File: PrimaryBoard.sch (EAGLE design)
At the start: 29 parts, among them J10 LORA32U4II, J11 CONN_42.54_SCREW, J13 POWER_JACK, J4 CONN_32.54_SCREW, J5 CONN_32.54_SCREW, J6 CONN_32.54_SCREW, J7 CONN_32.54_SCREW, J8 CONN_32.54_SCREW, J9 CONN_32.54_SCREW, U1 CD74HC4052PW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

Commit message: Minor updates and cleanup for primary board
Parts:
- added R2, R3: 10k, bschulz:R-EU_R0805
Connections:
- net 3V3_CORE: now also R2.2, R3.2
- net SCL: now also R3.1
- net SDA: now also R2.1
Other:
- note removed: "I2C Pullups!"
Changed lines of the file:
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@@
 <part name="C6" library="bschulz_passives" deviceset="C-EU" device="C0805"/>
 <part name="GND10" library="supply1" library_urn="urn:adsk.eagle:library:371" deviceset="GND" device=""/>
+<part name="R2" library="bschulz" deviceset="R-EU_" device="R0805" value="10k"/>
+<part name="R3" library="bschulz" deviceset="R-EU_" device="R0805" value="10k"/>
 </parts>
 <sheets>
 <sheet>
 <plain>
-<text x="78.74" y="102.87" size="1.778" layer="91">S0
+<text x="78.74" y="107.95" size="1.778" layer="91">S0
 S1
 IO_EN
@@
 LORA_EN
 5V_EXT_SENSE</text>
-<text x="78.74" y="99.06" size="1.778" layer="91">I2C Pullups!</text>
 </plain>
 <instances>
@@
 <instance part="GND10" gate="1" x="106.68" y="86.36" smashed="yes">
 <attribute name="VALUE" x="104.14" y="83.82" size="1.778" layer="96"/>
+</instance>
+<instance part="R2" gate="G$1" x="177.8" y="78.74" smashed="yes" rot="R90">
+<attribute name="NAME" x="176.3014" y="74.93" size="1.778" layer="95" rot="R90"/>
+<attribute name="VALUE" x="181.102" y="74.93" size="1.778" layer="96" rot="R90"/>
+</instance>
+<instance part="R3" gate="G$1" x="185.42" y="78.74" smashed="yes" rot="R90">
+<attribute name="NAME" x="183.9214" y="74.93" size="1.778" layer="95" rot="R90"/>
+<attribute name="VALUE" x="188.722" y="74.93" size="1.778" layer="96" rot="R90"/>
 </instance>
 </instances>
@@
 <wire x1="106.68" y1="99.06" x2="111.76" y2="99.06" width="0.1524" layer="91"/>
 </segment>
+<segment>
+<pinref part="R2" gate="G$1" pin="2"/>
+<wire x1="177.8" y1="83.82" x2="177.8" y2="86.36" width="0.1524" layer="91"/>
+<wire x1="177.8" y1="86.36" x2="185.42" y2="86.36" width="0.1524" layer="91"/>
+<pinref part="R3" gate="G$1" pin="2"/>
+<wire x1="185.42" y1="86.36" x2="185.42" y2="83.82" width="0.1524" layer="91"/>
+<wire x1="185.42" y1="86.36" x2="190.5" y2="86.36" width="0.1524" layer="91"/>
+<junction x="185.42" y="86.36"/>
+<label x="190.5" y="86.36" size="1.778" layer="95" xref="yes"/>
+</segment>
 </net>
 <net name="3V3_EXT" class="0">
@@
 <label x="129.54" y="83.82" size="1.778" layer="95"/>
 </segment>
+<segment>
+<pinref part="R2" gate="G$1" pin="1"/>
+<wire x1="177.8" y1="73.66" x2="177.8" y2="71.12" width="0.1524" layer="91"/>
+<wire x1="177.8" y1="71.12" x2="170.18" y2="71.12" width="0.1524" layer="91"/>
+<label x="170.18" y="71.12" size="1.778" layer="95"/>
+</segment>
 </net>
 <net name="SCL" class="0">
@@
 <label x="129.54" y="88.9" size="1.778" layer="95"/>
 </segment>
-</net>
+<segment>
+<pinref part="R3" gate="G$1" pin="1"/>
+<wire x1="185.42" y1="73.66" x2="185.42" y2="68.58" width="0.1524" layer="91"/>
+<wire x1="185.42" y1="68.58" x2="177.8" y2="68.58" width="0.1524" layer="91"/>
+<label x="177.8" y="68.58" size="1.778" layer="95"/>
+</segment>
+</net>

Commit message: Minor updates to Primary and Remote
Cleaned up/added silkscreen, added test points to both boards
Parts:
- added H1, H2, H3: (no value), bschulz:MOUNTING_HOLE2_NP
- added TP1, TP2, TP3, TP4, TP5, TP6: TESTPOINTRCU, bschulz:TESTPOINTRCU
- R2, R3: device bschulz:R-EU_R0805 -> bschulz_passives:R-EU_R0805
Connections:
- net GND: now also TP1.P$1
- net ONEWIRE: now also TP4.P$1
- net RX: now also TP6.P$1
- net SCL: now also TP3.P$1
- net SDA: now also TP2.P$1
- net TX: now also TP5.P$1
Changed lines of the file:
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@@
 <part name="C6" library="bschulz_passives" deviceset="C-EU" device="C0805"/>
 <part name="GND10" library="supply1" library_urn="urn:adsk.eagle:library:371" deviceset="GND" device=""/>
-<part name="R2" library="bschulz" deviceset="R-EU_" device="R0805" value="10k"/>
-<part name="R3" library="bschulz" deviceset="R-EU_" device="R0805" value="10k"/>
+<part name="R2" library="bschulz_passives" deviceset="R-EU_" device="R0805" value="10k"/>
+<part name="R3" library="bschulz_passives" deviceset="R-EU_" device="R0805" value="10k"/>
+<part name="H1" library="bschulz" deviceset="MOUNTING_HOLE" device="2_NP"/>
+<part name="H2" library="bschulz" deviceset="MOUNTING_HOLE" device="2_NP"/>
+<part name="H3" library="bschulz" deviceset="MOUNTING_HOLE" device="2_NP"/>
+<part name="TP1" library="bschulz" deviceset="TESTPOINT" device="RCU"/>
+<part name="TP2" library="bschulz" deviceset="TESTPOINT" device="RCU"/>
+<part name="TP3" library="bschulz" deviceset="TESTPOINT" device="RCU"/>
+<part name="TP4" library="bschulz" deviceset="TESTPOINT" device="RCU"/>
+<part name="TP5" library="bschulz" deviceset="TESTPOINT" device="RCU"/>
+<part name="TP6" library="bschulz" deviceset="TESTPOINT" device="RCU"/>
 </parts>
 <sheets>
@@
 <attribute name="VALUE" x="188.722" y="74.93" size="1.778" layer="96" rot="R90"/>
 </instance>
+<instance part="H1" gate="G$1" x="187.96" y="38.1" smashed="yes">
+<attribute name="NAME" x="189.992" y="38.6842" size="1.778" layer="95"/>
+<attribute name="VALUE" x="189.992" y="35.6362" size="1.778" layer="96"/>
+</instance>
+<instance part="H2" gate="G$1" x="187.96" y="30.48" smashed="yes">
+<attribute name="NAME" x="189.992" y="31.0642" size="1.778" layer="95"/>
+<attribute name="VALUE" x="189.992" y="28.0162" size="1.778" layer="96"/>
+</instance>
+<instance part="H3" gate="G$1" x="187.96" y="22.86" smashed="yes">
+<attribute name="NAME" x="189.992" y="23.4442" size="1.778" layer="95"/>
+<attribute name="VALUE" x="189.992" y="20.3962" size="1.778" layer="96"/>
+</instance>
+<instance part="TP1" gate="G$1" x="210.82" y="40.64" smashed="yes" rot="R90">
+<attribute name="NAME" x="207.01" y="38.1" size="1.27" layer="95" rot="R180" align="center"/>
+</instance>
+<instance part="TP2" gate="G$1" x="210.82" y="35.56" smashed="yes" rot="R90">
+<attribute name="NAME" x="207.01" y="33.02" size="1.27" layer="95" rot="R180" align="center"/>
+</instance>
+<instance part="TP3" gate="G$1" x="210.82" y="30.48" smashed="yes" rot="R90">
+<attribute name="NAME" x="207.01" y="27.94" size="1.27" layer="95" rot="R180" align="center"/>
+</instance>
+<instance part="TP4" gate="G$1" x="210.82" y="22.86" smashed="yes" rot="R90">
+<attribute name="NAME" x="207.01" y="20.32" size="1.27" layer="95" rot="R180" align="center"/>
+</instance>
+<instance part="TP5" gate="G$1" x="210.82" y="17.78" smashed="yes" rot="R90">
+<attribute name="NAME" x="207.01" y="15.24" size="1.27" layer="95" rot="R180" align="center"/>
+</instance>
+<instance part="TP6" gate="G$1" x="210.82" y="12.7" smashed="yes" rot="R90">
+<attribute name="NAME" x="207.01" y="10.16" size="1.27" layer="95" rot="R180" align="center"/>
+</instance>
 </instances>
 <busses>
@@
 <pinref part="GND10" gate="1" pin="GND"/>
 </segment>
+<segment>
+<pinref part="TP1" gate="G$1" pin="P$1"/>
+<wire x1="210.82" y1="40.64" x2="218.44" y2="40.64" width="0.1524" layer="91"/>
+<label x="213.36" y="40.64" size="1.778" layer="95"/>
+</segment>
 </net>
 <net name="N$2" class="0">
@@
 <label x="170.18" y="71.12" size="1.778" layer="95"/>
 </segment>
+<segment>
+<pinref part="TP2" gate="G$1" pin="P$1"/>
+<wire x1="210.82" y1="35.56" x2="218.44" y2="35.56" width="0.1524" layer="91"/>
+<label x="213.36" y="35.56" size="1.778" layer="95"/>
+</segment>
 </net>
 <net name="SCL" class="0">
@@
 <label x="177.8" y="68.58" size="1.778" layer="95"/>
 </segment>
+<segment>
+<pinref part="TP3" gate="G$1" pin="P$1"/>
+<wire x1="210.82" y1="30.48" x2="218.44" y2="30.48" width="0.1524" layer="91"/>
+<label x="213.36" y="30.48" size="1.778" layer="95"/>
+</segment>
 </net>
 <net name="ONEWIRE" class="0">
@@
 <label x="73.66" y="91.44" size="1.778" layer="95"/>
 </segment>
+<segment>
+<pinref part="TP4" gate="G$1" pin="P$1"/>
+<wire x1="210.82" y1="22.86" x2="218.44" y2="22.86" width="0.1524" layer="91"/>
+<label x="213.36" y="22.86" size="1.778" layer="95"/>
+</segment>
 </net>
 <net name="TX" class="0">
@@
 <label x="130.81" y="25.4" size="1.778" layer="95"/>
 </segment>
+<segment>
+<pinref part="TP5" gate="G$1" pin="P$1"/>
+<wire x1="210.82" y1="17.78" x2="218.44" y2="17.78" width="0.1524" layer="91"/>
+<label x="213.36" y="17.78" size="1.778" layer="95"/>
+</segment>
 </net>
 <net name="RX" class="0">
@@
 <label x="130.81" y="27.94" size="1.778" layer="95"/>
 </segment>
-</net>
+<segment>
+<pinref part="TP6" gate="G$1" pin="P$1"/>
+<wire x1="210.82" y1="12.7" x2="218.44" y2="12.7" width="0.1524" layer="91"/>
+<label x="213.36" y="12.7" size="1.778" layer="95"/>
+</segment>
+</net>

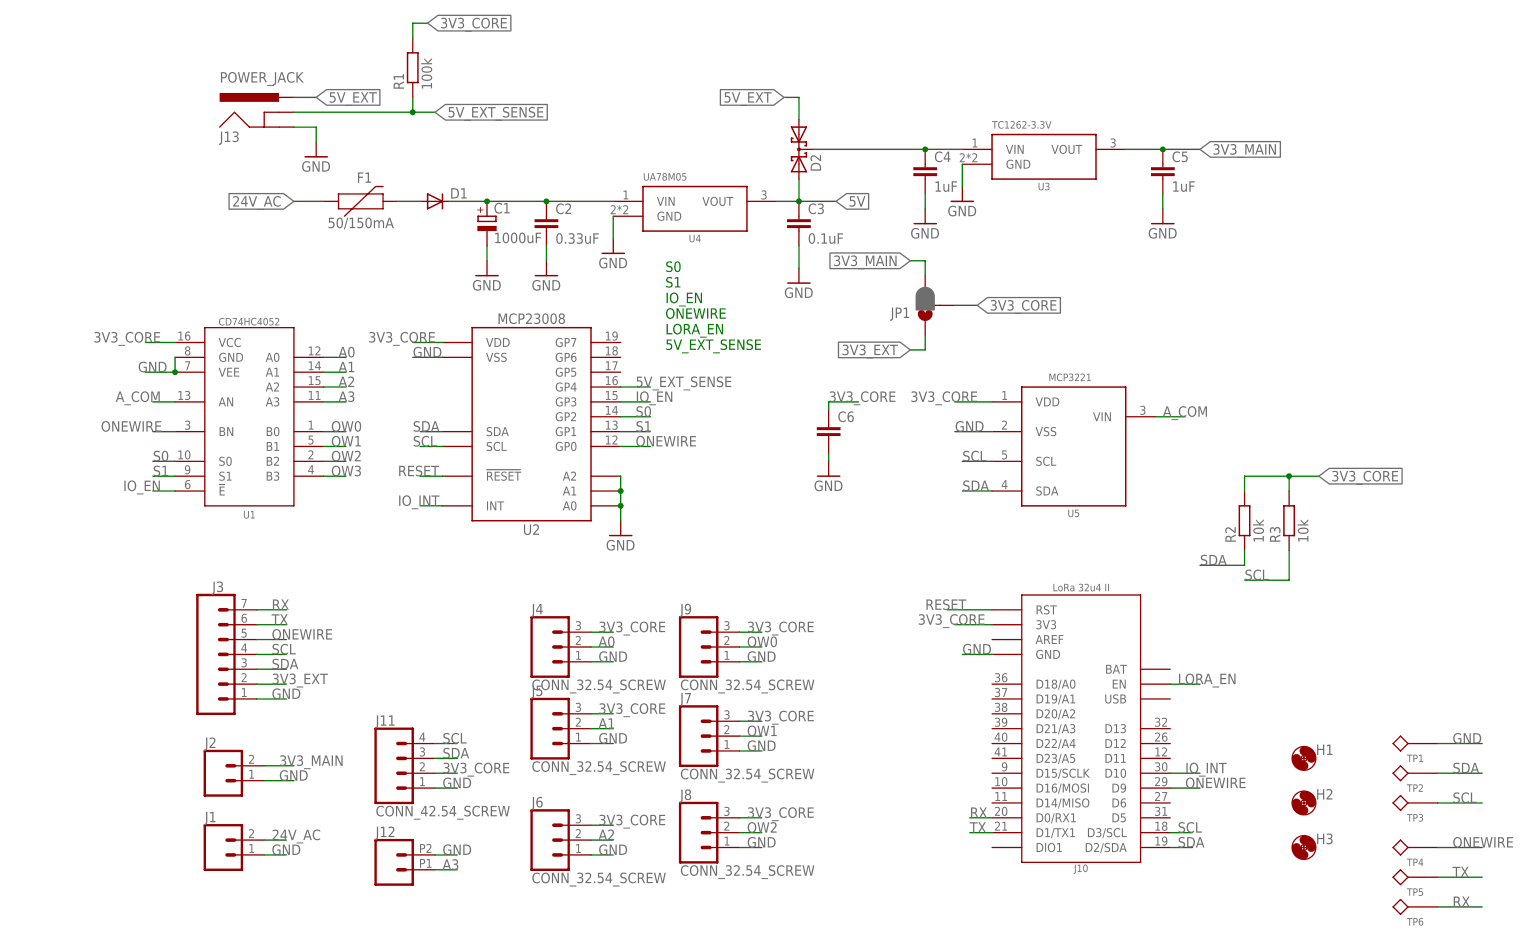
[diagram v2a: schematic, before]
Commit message: Minor cleanup/fixes to boards, generated gerbers
Minor changes to boards, primarily cleanup and generated gerbers for fab, ready for review
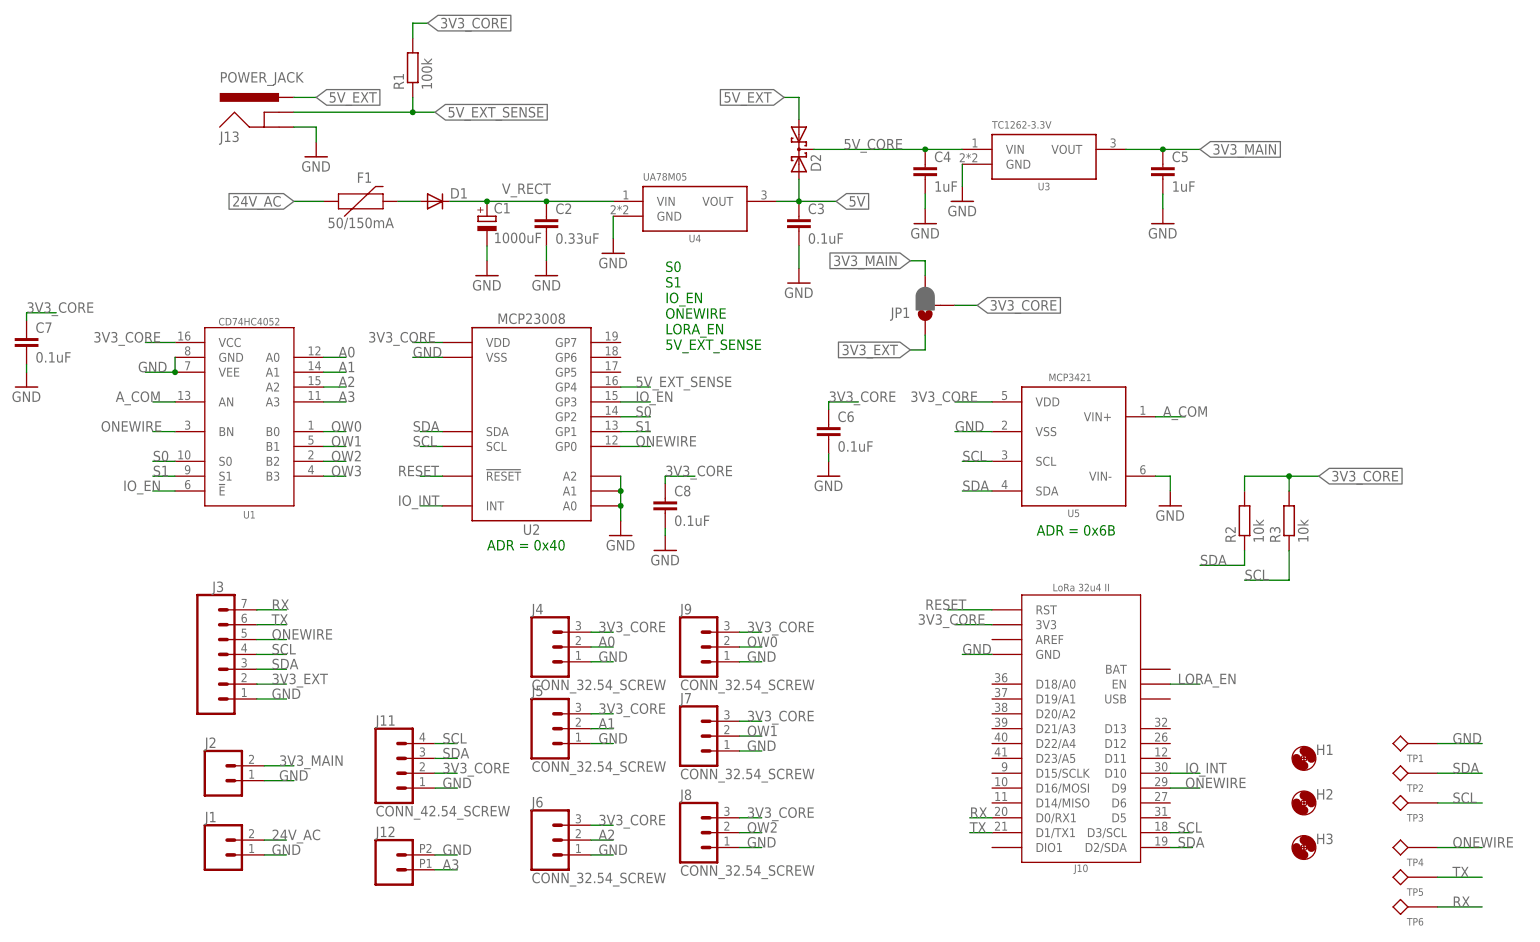
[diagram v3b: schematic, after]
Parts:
- added C7, C8: 0.1uF, bschulz_passives:C-EUC0805
- C6: value (none) -> 0.1uF
- U5: value MCP3221 -> MCP3421A3; device bschulz:MCP3221 -> bschulz:MCP3421A3
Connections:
- net N$1 renamed 5V_CORE
- net N$2 renamed V_RECT
- net 3V3_CORE: now also C7.1, C8.1
- net A_COM: now also U5.VIN+; no longer U5.VIN
- net GND: now also C7.2, C8.2, U5.VIN-
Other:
- note added: "ADR = 0x40"
- note added: "ADR = 0x6B"
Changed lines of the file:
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@@
 <part name="J7" library="bschulz" deviceset="CONN_3" device="2.54_SCREW"/>
 <part name="J8" library="bschulz" deviceset="CONN_3" device="2.54_SCREW"/>
-<part name="U5" library="bschulz" deviceset="MCP3221" device=""/>
-<part name="C6" library="bschulz_passives" deviceset="C-EU" device="C0805"/>
+<part name="U5" library="bschulz" deviceset="MCP342*" device="" technology="1A3" value="MCP3421A3"/>
+<part name="C6" library="bschulz_passives" deviceset="C-EU" device="C0805" value="0.1uF"/>
 <part name="GND10" library="supply1" library_urn="urn:adsk.eagle:library:371" deviceset="GND" device=""/>
 <part name="R2" library="bschulz_passives" deviceset="R-EU_" device="R0805" value="10k"/>
@@
 <part name="TP5" library="bschulz" deviceset="TESTPOINT" device="RCU"/>
 <part name="TP6" library="bschulz" deviceset="TESTPOINT" device="RCU"/>
+<part name="C7" library="bschulz_passives" deviceset="C-EU" device="C0805" value="0.1uF"/>
+<part name="GND11" library="supply1" library_urn="urn:adsk.eagle:library:371" deviceset="GND" device=""/>
+<part name="C8" library="bschulz_passives" deviceset="C-EU" device="C0805" value="0.1uF"/>
+<part name="GND12" library="supply1" library_urn="urn:adsk.eagle:library:371" deviceset="GND" device=""/>
+<part name="GND13" library="supply1" library_urn="urn:adsk.eagle:library:371" deviceset="GND" device=""/>
 </parts>
 <sheets>
@@
 LORA_EN
 5V_EXT_SENSE</text>
+<text x="142.24" y="76.2" size="1.778" layer="91">ADR = 0x6B</text>
+<text x="48.26" y="73.66" size="1.778" layer="91">ADR = 0x40</text>
 </plain>
 <instances>
@@
 <instance part="TP6" gate="G$1" x="210.82" y="12.7" smashed="yes" rot="R90">
 <attribute name="NAME" x="207.01" y="10.16" size="1.27" layer="95" rot="R180" align="center"/>
+</instance>
+<instance part="C7" gate="G$1" x="-30.48" y="110.49" smashed="yes">
+<attribute name="NAME" x="-28.956" y="110.871" size="1.778" layer="95"/>
+<attribute name="VALUE" x="-28.956" y="105.791" size="1.778" layer="96"/>
+</instance>
+<instance part="GND11" gate="1" x="-30.48" y="101.6" smashed="yes">
+<attribute name="VALUE" x="-33.02" y="99.06" size="1.778" layer="96"/>
+</instance>
+<instance part="C8" gate="G$1" x="78.74" y="82.55" smashed="yes">
+<attribute name="NAME" x="80.264" y="82.931" size="1.778" layer="95"/>
+<attribute name="VALUE" x="80.264" y="77.851" size="1.778" layer="96"/>
+</instance>
+<instance part="GND12" gate="1" x="78.74" y="73.66" smashed="yes">
+<attribute name="VALUE" x="76.2" y="71.12" size="1.778" layer="96"/>
+</instance>
+<instance part="GND13" gate="1" x="165.1" y="81.28" smashed="yes">
+<attribute name="VALUE" x="162.56" y="78.74" size="1.778" layer="96"/>
 </instance>
 </instances>
@@
 <label x="213.36" y="40.64" size="1.778" layer="95"/>
 </segment>
-</net>
-<net name="N$2" class="0">
+<segment>
+<pinref part="C7" gate="G$1" pin="2"/>
+<wire x1="-30.48" y1="105.41" x2="-30.48" y2="104.14" width="0.1524" layer="91"/>
+<pinref part="GND11" gate="1" pin="GND"/>
+</segment>
+<segment>
+<pinref part="C8" gate="G$1" pin="2"/>
+<wire x1="78.74" y1="77.47" x2="78.74" y2="76.2" width="0.1524" layer="91"/>
+<pinref part="GND12" gate="1" pin="GND"/>
+</segment>
+<segment>
+<pinref part="GND13" gate="1" pin="GND"/>
+<wire x1="165.1" y1="83.82" x2="165.1" y2="86.36" width="0.1524" layer="91"/>
+<pinref part="U5" gate="G$1" pin="VIN-"/>
+<wire x1="165.1" y1="86.36" x2="162.56" y2="86.36" width="0.1524" layer="91"/>
+</segment>
+</net>
+<net name="V_RECT" class="0">
 <segment>
 <pinref part="D1" gate="G$1" pin="C"/>
@@
 <junction x="48.26" y="133.35"/>
 <junction x="58.42" y="133.35"/>
+<label x="50.8" y="134.62" size="1.778" layer="95"/>
 </segment>
 </net>
@@
 </segment>
 </net>
-<net name="N$1" class="0">
+<net name="5V_CORE" class="0">
 <segment>
 <pinref part="D2" gate="G$1" pin="C"/>
@@
 <wire x1="123.19" y1="142.24" x2="129.54" y2="142.24" width="0.1524" layer="91"/>
 <junction x="123.19" y="142.24"/>
+<label x="109.22" y="142.24" size="1.778" layer="95"/>
 </segment>
 </net>
@@
 <label x="190.5" y="86.36" size="1.778" layer="95" xref="yes"/>
 </segment>
+<segment>
+<pinref part="C7" gate="G$1" pin="1"/>
+<wire x1="-30.48" y1="113.03" x2="-30.48" y2="114.3" width="0.1524" layer="91"/>
+<label x="-30.48" y="114.3" size="1.778" layer="95"/>
+<wire x1="-30.48" y1="114.3" x2="-25.4" y2="114.3" width="0.1524" layer="91"/>
+</segment>
+<segment>
+<pinref part="C8" gate="G$1" pin="1"/>
+<wire x1="78.74" y1="85.09" x2="78.74" y2="86.36" width="0.1524" layer="91"/>
+<label x="78.74" y="86.36" size="1.778" layer="95"/>
+<wire x1="78.74" y1="86.36" x2="83.82" y2="86.36" width="0.1524" layer="91"/>
+</segment>
 </net>
 <net name="3V3_EXT" class="0">
@@
 </segment>
 <segment>
-<pinref part="U5" gate="G$1" pin="VIN"/>
+<pinref part="U5" gate="G$1" pin="VIN+"/>
 <wire x1="162.56" y1="96.52" x2="167.64" y2="96.52" width="0.1524" layer="91"/>
 <label x="163.83" y="96.52" size="1.778" layer="95"/>
